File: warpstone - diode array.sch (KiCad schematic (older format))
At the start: 89 parts, among them SW1 SW_Push, U1 ProMicro

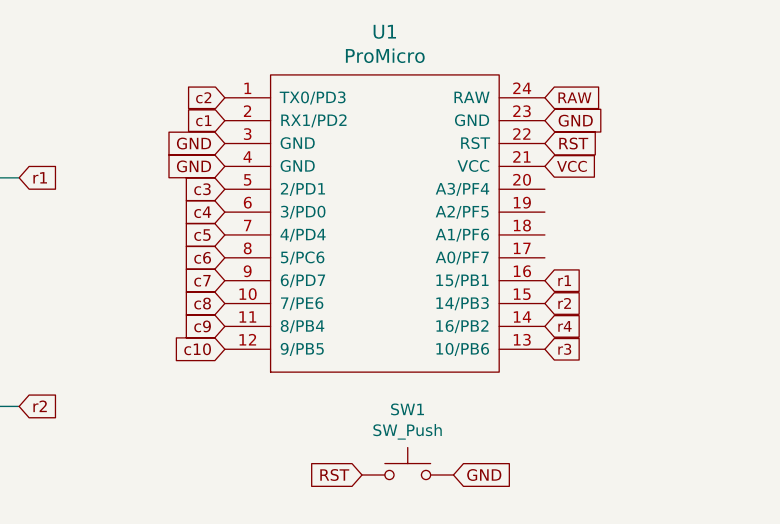
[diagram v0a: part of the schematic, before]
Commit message: overhaul
total overhaul to the design of the board
case design now available
protos en route
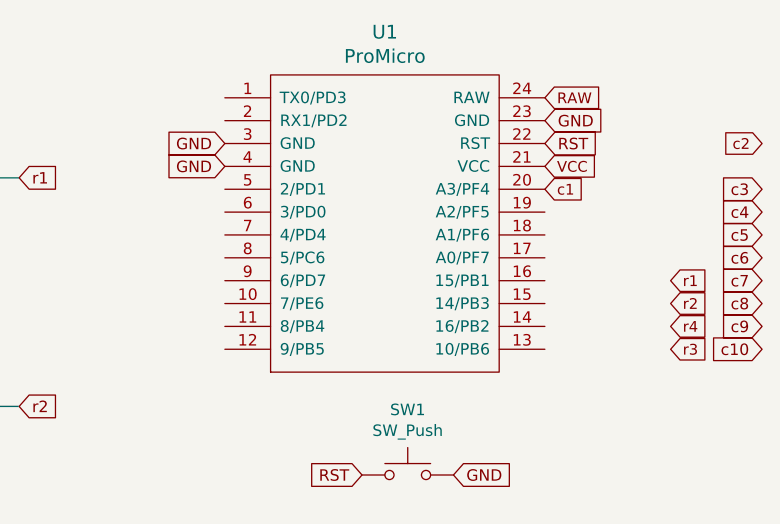
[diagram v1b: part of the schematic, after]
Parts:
- D1, D10, D11, D12, D13, D14, D15, D16, D17, D18, D19, D2, D20, D21, D22, D23, D24, D25, D26, D27, D28, D29, D3, D30, D31, D32, D33, D34, D35, D36, D37, D38, D4, D5, D6, D7, D8, D9: footprint Keebio-Parts:Diode-Hybrid-Back -> Keebio-Parts:D_SOD123
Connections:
- net c1: now also U1.20 (A3/PF4); no longer U1.2 (RX1/PD2)
- net c10: no longer U1.12 (9/PB5)
- net c2: no longer U1.1 (TX0/PD3)
- net c3: no longer U1.5 (2/PD1)
- net c4: no longer U1.6 (3/PD0)
- net c5: no longer U1.7 (4/PD4)
- net c6: no longer U1.8 (5/PC6)
- net c7: no longer U1.9 (6/PD7)
- net c8: no longer U1.10 (7/PE6)
- net c9: no longer U1.11 (8/PB4)
- net r1: no longer U1.16 (15/PB1)
- net r2: no longer U1.15 (14/PB3)
- net r3: no longer U1.13 (10/PB6)
- net r4: no longer U1.14 (16/PB2)
